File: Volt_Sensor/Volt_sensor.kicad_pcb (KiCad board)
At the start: 2 copper layers, 150 x 71 mm, 28 parts, among them P1 CONN_01X03, P2 CONN_01X02, P3 CONN_01X02, P4 CONN_01X02, U1 LV-25-P, U2 NE5532

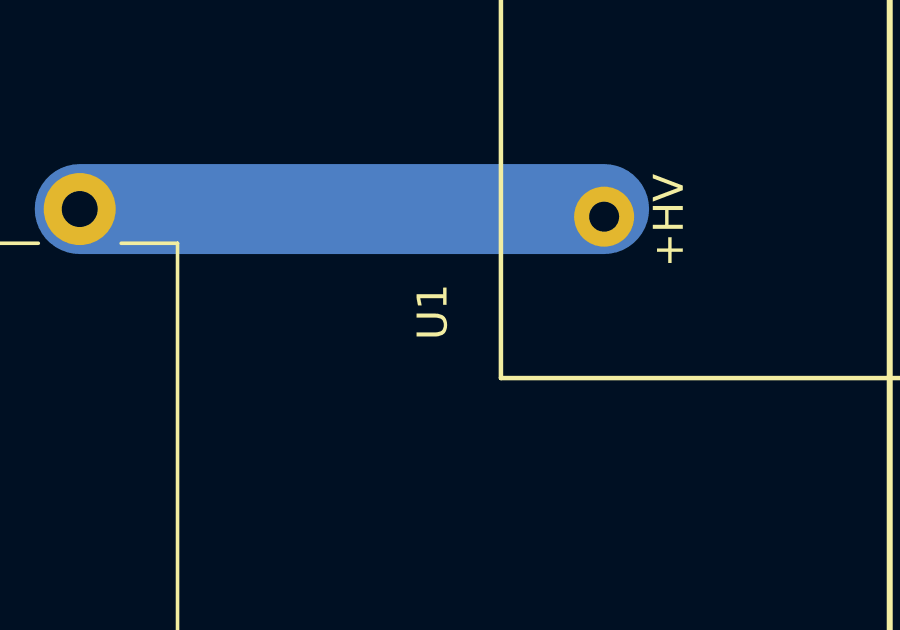
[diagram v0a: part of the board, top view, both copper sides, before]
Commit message: Updated LEM footprint
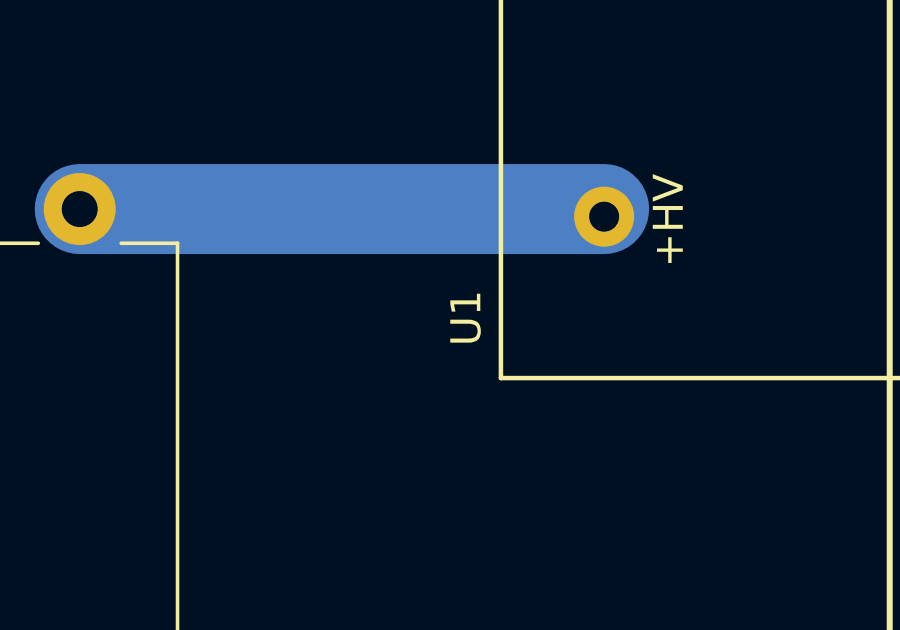
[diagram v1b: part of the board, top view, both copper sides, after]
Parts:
- U1: footprint LEM:LV25-P -> Hall-Effect_Transducers_LEM:LV25-P
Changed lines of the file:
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@@
     (links 39)
     (no_connects 0)
-    (area 84.197 60.622201 249.764568 140.2066)
+    (area 87.924999 64.924999 238.075001 136.075001)
     (thickness 1.6)
     (drawings 41)
@@
       (at (xyz 0 0 0))
       (scale (xyz 0.393701 0.393701 0.393701))
-      (rotate (xyz 0 0 0))
-    )
-  )
-  (module LEM:LV25-P (layer F.Cu)
-    (at 167.64 100.584 90)
-    (fp_text reference U1 (at -10.795 -15.875 90) (layer F.SilkS)
-      (effects (font (size 1 1) (thickness 0.15)))
-    )
-    (fp_text value LV-25-P (at 10.16 15.875 90) (layer F.Fab)
-      (effects (font (size 1 1) (thickness 0.15)))
-    )
-    (fp_text user M (at 7.75 12.5 90) (layer F.SilkS)
-      (effects (font (size 1 1) (thickness 0.15)))
-    )
-    (fp_text user + (at 0 12.5 90) (layer F.SilkS)
-      (effects (font (size 1 1) (thickness 0.15)))
-    )
-    (fp_text user - (at -7.75 12.5 90) (layer F.SilkS)
-      (effects (font (size 1 1) (thickness 0.15)))
-    )
-    (fp_text user -HV (at 7 -7.75 90) (layer F.SilkS)
-      (effects (font (size 1 1) (thickness 0.15)))
-    )
-    (fp_text user +HV (at -7.75 -8 90) (layer F.SilkS)
-      (effects (font (size 1 1) (thickness 0.15)))
-    )
-    (fp_line (start -13 -13.6) (end -13 15.6) (layer F.SilkS) (width 0.15))
-    (fp_line (start 13 -13.6) (end 13 15.6) (layer F.SilkS) (width 0.15))
-    (fp_line (start -13 -13.6) (end 13 -13.6) (layer F.SilkS) (width 0.15))
-    (fp_line (start -13 15.6) (end 13 15.6) (layer F.SilkS) (width 0.15))
-    (pad 1 thru_hole circle (at -7.62 -10.16 90) (size 2 2) (drill 1) (layers *.Cu *.Mask)
-      (net 10 "Net-(R5-Pad1)"))
-    (pad 2 thru_hole circle (at 7.62 -10.16 90) (size 2 2) (drill 1) (layers *.Cu *.Mask)
-      (net 11 "Net-(R6-Pad1)"))
-    (pad 3 thru_hole circle (at -7.62 10.16 90) (size 2.5 2.5) (drill 1.2) (layers *.Cu *.Mask)
-      (net 1 VCC))
-    (pad 4 thru_hole circle (at 0 10.16 90) (size 2.5 2.5) (drill 1.2) (layers *.Cu *.Mask)
-      (net 15 "Net-(P3-Pad1)"))
-    (pad 5 thru_hole circle (at 7.62 10.16 90) (size 2.5 2.5) (drill 1.2) (layers *.Cu *.Mask)
-      (net 3 VEE))
-    (model /Users/Yngve/git/Switchcraft/kicad-lib/packages3d/LEM.3dshapes/LV25-P.wrl
-      (at (xyz 0 0 0))
-      (scale (xyz 1 1 1))
       (rotate (xyz 0 0 0))
     )
@@
     (pad "" np_thru_hole circle (at 0 0) (size 5 5) (drill 4.3) (layers *.Cu *.Mask))
   )
+  (module Hall-Effect_Transducers_LEM:LV25-P (layer F.Cu)
+    (at 167.64 100.584 90)
+    (fp_text reference U1 (at -11 -14.75 90) (layer F.SilkS)
+      (effects (font (size 1 1) (thickness 0.15)))
+    )
+    (fp_text value LV-25-P (at 10.25 17 90) (layer F.Fab)
+      (effects (font (size 1 1) (thickness 0.15)))
+    )
+    (fp_text user M (at 7.75 12.5 90) (layer F.SilkS)
+      (effects (font (size 1 1) (thickness 0.15)))
+    )
+    (fp_text user + (at 0 12.5 90) (layer F.SilkS)
+      (effects (font (size 1 1) (thickness 0.15)))
+    )
+    (fp_text user - (at -7.75 12.5 90) (layer F.SilkS)
+      (effects (font (size 1 1) (thickness 0.15)))
+    )
+    (fp_text user -HV (at 7 -7.75 90) (layer F.SilkS)
+      (effects (font (size 1 1) (thickness 0.15)))
+    )
+    (fp_text user +HV (at -7.75 -8 90) (layer F.SilkS)
+      (effects (font (size 1 1) (thickness 0.15)))
+    )
+    (fp_line (start -13 -13.6) (end -13 15.6) (layer F.SilkS) (width 0.15))
+    (fp_line (start 13 -13.6) (end 13 15.6) (layer F.SilkS) (width 0.15))
+    (fp_line (start -13 -13.6) (end 13 -13.6) (layer F.SilkS) (width 0.15))
+    (fp_line (start -13 15.6) (end 13 15.6) (layer F.SilkS) (width 0.15))
+    (pad 1 thru_hole circle (at -7.62 -10.16 90) (size 2 2) (drill 1) (layers *.Cu *.Mask)
+      (net 10 "Net-(R5-Pad1)"))
+    (pad 2 thru_hole circle (at 7.62 -10.16 90) (size 2 2) (drill 1) (layers *.Cu *.Mask)
+      (net 11 "Net-(R6-Pad1)"))
+    (pad 3 thru_hole circle (at -7.62 10.16 90) (size 2.5 2.5) (drill 1.2) (layers *.Cu *.Mask)
+      (net 1 VCC))
+    (pad 4 thru_hole circle (at 0 10.16 90) (size 2.5 2.5) (drill 1.2) (layers *.Cu *.Mask)
+      (net 15 "Net-(P3-Pad1)"))
+    (pad 5 thru_hole circle (at 7.62 10.16 90) (size 2.5 2.5) (drill 1.2) (layers *.Cu *.Mask)
+      (net 3 VEE))
+    (model /Users/Yngve/git/Switchcraft/kicad-lib/packages3d/LEM.3dshapes/LV25-P.wrl
+      (at (xyz 0 0 0))
+      (scale (xyz 1 1 1))
+      (rotate (xyz 0 0 0))
+    )
+  )
   (gr_text "what's my purpose...?" (at 221.1832 66.7766) (layer B.SilkS)

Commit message: Changed pot meter
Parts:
- RV1, RV2: footprint potentiometer:Potentiometer_Trimmer-Suntan-TSR-3386P -> Potentiometers:Potentiometer_Trimmer_ACP_CA6v_Horizontal
- moved RV1 0.11 mm to (190.0, 97.0), turned to 0 degrees
- moved RV2 0.08 mm to (190.0, 107.5), turned to 0 degrees
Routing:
- net Net-(RV1-Pad2): track 10.1 -> 7.49 mm
- net Net-(P4-Pad1): track 48.3 -> 49.1 mm
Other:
- board text removed: "Danger Primary Voltage Area"

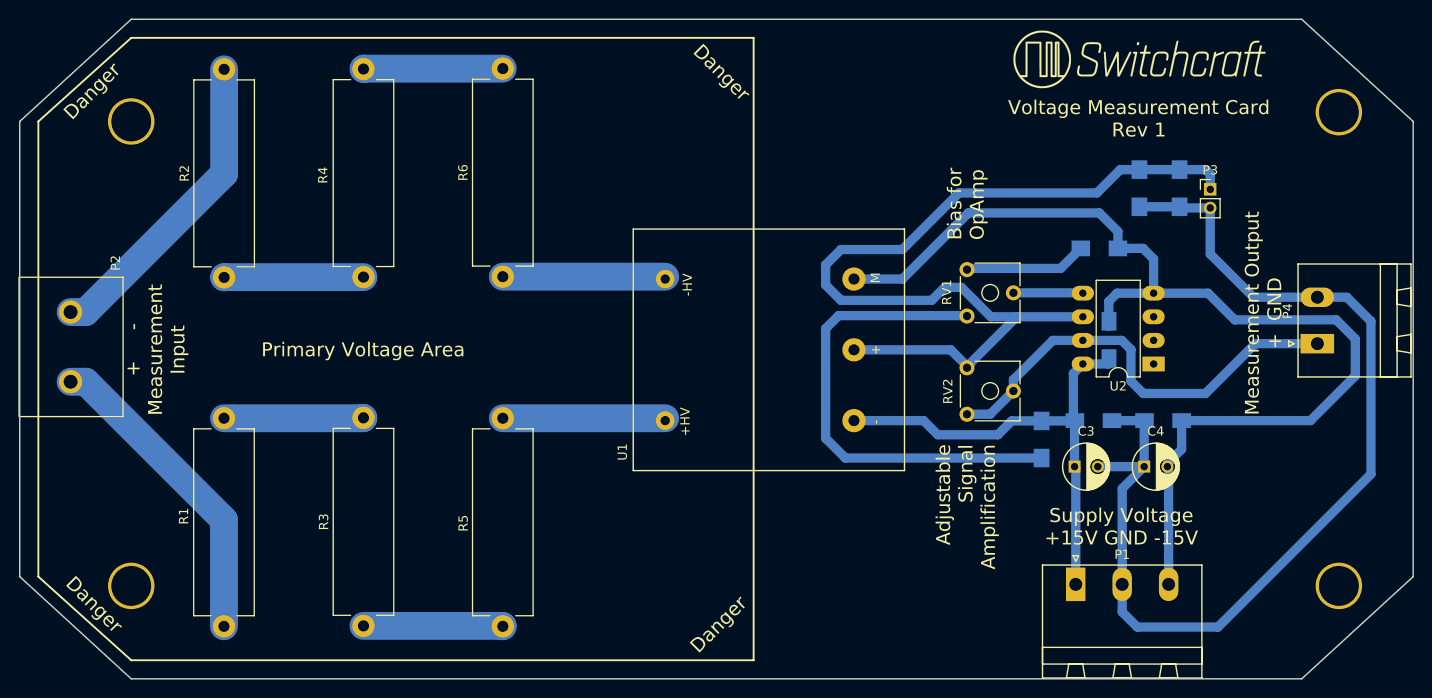
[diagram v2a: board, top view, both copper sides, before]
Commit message: Updated current sensor card
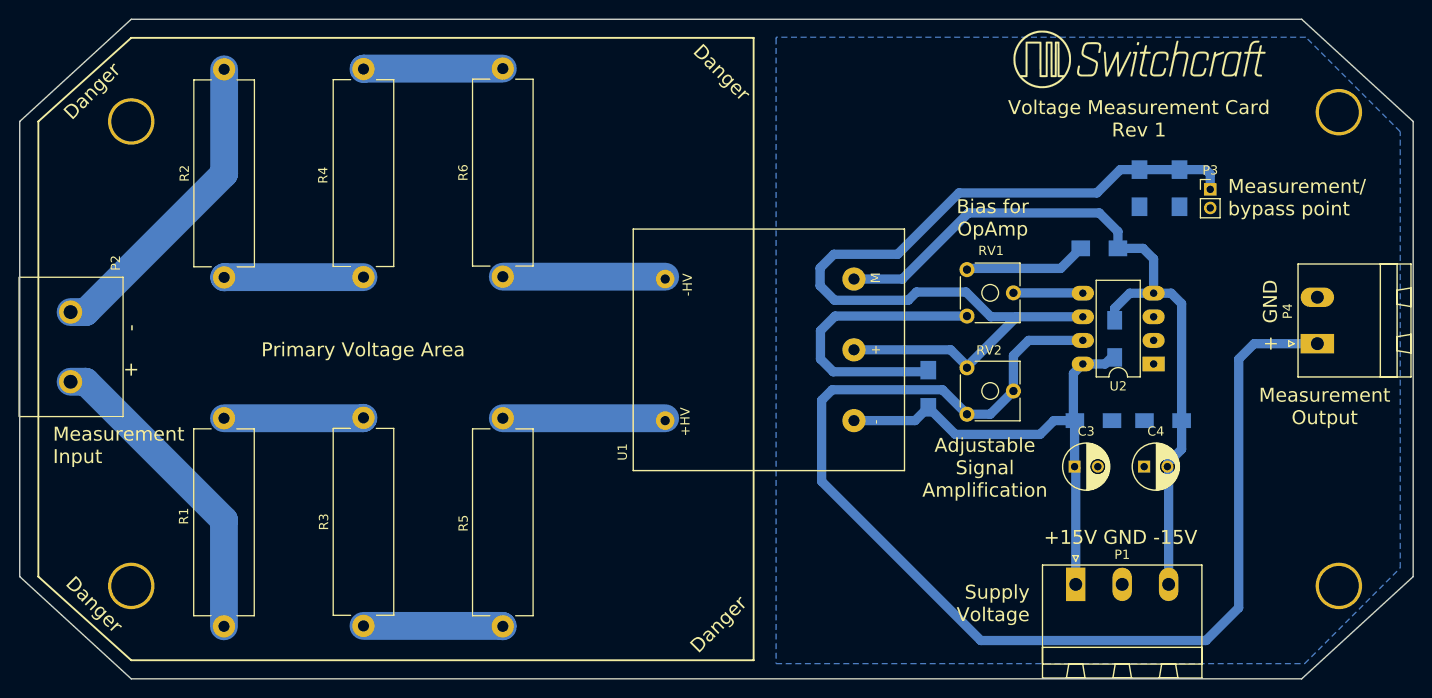
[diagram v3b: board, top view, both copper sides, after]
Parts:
- moved R8 13.4 mm to (185.8, 104.8), turned to 90 degrees
- moved C5 0.62 mm to (205.9, 99.4)
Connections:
- REF** pad : (no net) -> GND (x2)
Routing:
- net GND: track 113.7 -> 0.05 mm
- net Net-(P4-Pad1): track 49.1 -> 133.3 mm
- net VEE: track 117.7 -> 82.7 mm
- net Net-(R8-Pad2): track 51.6 -> 31.7 mm
- net VCC: track 52.2 -> 54.0 mm
- net Net-(P3-Pad1): track 100.4 -> 101.0 mm
- added copper zone on B.Cu, net GND
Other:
- board text added: "+ -"
- board text added: "+ GND"
- board text added: "+15V GND -15V"
- board text added: "Measurement Input"
- board text added: "Measurement Output"
- board text added: "Measurement/ bypass point"
- board text added: "Supply Voltage"
- board text removed: "+ - Measurement Input"
- board text removed: "Measurement Output + GND"
- board text removed: "Supply Voltage +15V GND -15V"

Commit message: Finalized - Ready for production
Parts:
- added REF***: OSHW-Logo2_7.3x6mm_SilkScreen, OSHW:OSHW-Logo2_7.3x6mm_SilkScreen, F.Cu at (214.2, 70.5)
- moved G*** 19.1 mm to (189.6, 69.5)
